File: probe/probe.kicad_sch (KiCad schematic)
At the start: 4 parts, among them J1 To circuit, J2 To scope

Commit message: Update based on first constructed version
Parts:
- added C2: 5pF, Capacitor_SMD:C_0805_2012Metric, symbol Device:C
- added R2: 4.5MΩ, Resistor_SMD:R_0805_2012Metric_Pad1.20x1.40mm_HandSolder, symbol Device:R
- R1: value 9MΩ -> 4.5MΩ
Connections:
- net In: now reaches C1.1, J1.1 (In), R1.1
- net In: now also C2.1
- net Out: now reaches C1.2, J2.1 (In)
- net Out: now also C2.2, R2.2; no longer R1.2
- new net: R1.2, R2.1
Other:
- moved on the sheet: R1
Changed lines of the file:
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@@
 	(paper "A4")
+	(junction
+		(at 119.38 87.63)
+		(diameter 0)
+		(color 0 0 0 0)
+	)
 	(junction
 		(at 119.38 80.01)
@@
 		(color 0 0 0 0)
 	)
+	(junction
+		(at 138.43 87.63)
+		(diameter 0)
+		(color 0 0 0 0)
+	)
 	(wire
 		(pts
@@
 	(wire
 		(pts
-			(xy 119.38 80.01) (xy 124.46 80.01)
+			(xy 119.38 80.01) (xy 120.65 80.01)
 		)
 		(stroke
@@
 	(wire
 		(pts
+			(xy 132.08 97.79) (xy 138.43 97.79)
+		)
+		(stroke
+			(width 0)
+			(type default)
+		)
+	)
+	(wire
+		(pts
 			(xy 119.38 80.01) (xy 119.38 87.63)
 		)
@@
 	(wire
 		(pts
-			(xy 132.08 80.01) (xy 138.43 80.01)
+			(xy 138.43 87.63) (xy 138.43 97.79)
+		)
+		(stroke
+			(width 0)
+			(type default)
+		)
+	)
+	(wire
+		(pts
+			(xy 128.27 80.01) (xy 129.54 80.01)
+		)
+		(stroke
+			(width 0)
+			(type default)
+		)
+	)
+	(wire
+		(pts
+			(xy 119.38 87.63) (xy 119.38 97.79)
+		)
+		(stroke
+			(width 0)
+			(type default)
+		)
+	)
+	(wire
+		(pts
+			(xy 124.46 97.79) (xy 119.38 97.79)
 		)
 		(stroke
@@
 	(wire
 		(pts
+			(xy 137.16 80.01) (xy 138.43 80.01)
+		)
+		(stroke
+			(width 0)
+			(type default)
+		)
+	)
+	(wire
+		(pts
 			(xy 152.4 85.09) (xy 152.4 90.17)
 		)
@@
 			(width 0)
 			(type default)
+		)
+	)
+	(label "In"
+		(at 111.76 80.01 0)
+		(effects
+			(font
+				(size 1.27 1.27)
+			)
+			(justify left bottom)
+		)
+	)
+	(label "Out"
+		(at 140.97 80.01 0)
+		(effects
+			(font
+				(size 1.27 1.27)
+			)
+			(justify left bottom)
 		)
 	)
@@
 	)
 	(symbol
+		(lib_id "Device:R")
+		(at 133.35 80.01 90)
+		(unit 1)
+		(exclude_from_sim no)
+		(in_bom yes)
+		(on_board yes)
+		(dnp no)
+		(fields_autoplaced yes)
+		(property "Reference" "R2"
+			(at 133.35 73.66 90)
+			(effects
+				(font
+					(size 1.27 1.27)
+				)
+			)
+		)
+		(property "Value" "4.5MΩ"
+			(at 133.35 76.2 90)
+			(effects
+				(font
+					(size 1.27 1.27)
+				)
+			)
+		)
+		(property "Footprint" "Resistor_SMD:R_0805_2012Metric_Pad1.20x1.40mm_HandSolder"
+			(at 133.35 81.788 90)
+			(effects
+				(font
+					(size 1.27 1.27)
+				)
+				(hide yes)
+			)
+		)
+		(property "Datasheet" "~"
+			(at 133.35 80.01 0)
+			(effects
+				(font
+					(size 1.27 1.27)
+				)
+				(hide yes)
+			)
+		)
+		(property "Description" "Resistor"
+			(at 133.35 80.01 0)
+			(effects
+				(font
+					(size 1.27 1.27)
+				)
+				(hide yes)
+			)
+		)
+		(pin "2"
+		)
+		(pin "1"
+		)
+		(instances
+			(project "probe"
+				(path "/0e2e18e6-1bf7-45b9-957f-fc4f8daaef3f"
+					(reference "R2")
+					(unit 1)
+				)
+			)
+		)
+	)
+	(symbol
 		(lib_id "power:GND")
 		(at 152.4 90.17 0)
@@
 	)
 	(symbol
+		(lib_id "Device:C")
+		(at 128.27 97.79 90)
+		(unit 1)
+		(exclude_from_sim no)
+		(in_bom yes)
+		(on_board yes)
+		(dnp no)
+		(property "Reference" "C2"
+			(at 128.27 101.6 90)
+			(effects
+				(font
+					(size 1.27 1.27)
+				)
+			)
+		)
+		(property "Value" "5pF"
+			(at 128.524 103.632 90)
+			(effects
+				(font
+					(size 1.27 1.27)
+				)
+			)
+		)
+		(property "Footprint" "Capacitor_SMD:C_0805_2012Metric"
+			(at 132.08 96.8248 0)
+			(effects
+				(font
+					(size 1.27 1.27)
+				)
+				(hide yes)
+			)
+		)
+		(property "Datasheet" "~"
+			(at 128.27 97.79 0)
+			(effects
+				(font
+					(size 1.27 1.27)
+				)
+				(hide yes)
+			)
+		)
+		(property "Description" "Unpolarized capacitor"
+			(at 128.27 97.79 0)
+			(effects
+				(font
+					(size 1.27 1.27)
+				)
+				(hide yes)
+			)
+		)
+		(pin "1"
+		)
+		(pin "2"
+		)
+		(instances
+			(project "probe"
+				(path "/0e2e18e6-1bf7-45b9-957f-fc4f8daaef3f"
+					(reference "C2")
+					(unit 1)
+				)
+			)
+		)
+	)
+	(symbol
 		(lib_id "Device:R")
-		(at 128.27 80.01 90)
+		(at 124.46 80.01 90)
 		(unit 1)
 		(exclude_from_sim no)
@@
 		(fields_autoplaced yes)
 		(property "Reference" "R1"
-			(at 128.27 73.66 90)
-			(effects
-				(font
-					(size 1.27 1.27)
-				)
-			)
-		)
-		(property "Value" "9MΩ"
-			(at 128.27 76.2 90)
+			(at 124.46 73.66 90)
+			(effects
+				(font
+					(size 1.27 1.27)
+				)
+			)
+		)
+		(property "Value" "4.5MΩ"
+			(at 124.46 76.2 90)
 			(effects
 				(font
@@
 		)
 		(property "Footprint" "Resistor_SMD:R_0805_2012Metric_Pad1.20x1.40mm_HandSolder"
-			(at 128.27 81.788 90)
+			(at 124.46 81.788 90)
 			(effects
 				(font
@@
 		)
 		(property "Datasheet" "~"
-			(at 128.27 80.01 0)
+			(at 124.46 80.01 0)
 			(effects
 				(font
@@
 		)
 		(property "Description" "Resistor"
-			(at 128.27 80.01 0)
-			(effects
-				(font
+			(at 124.46 80.01 0)
+			(effects
+				(font

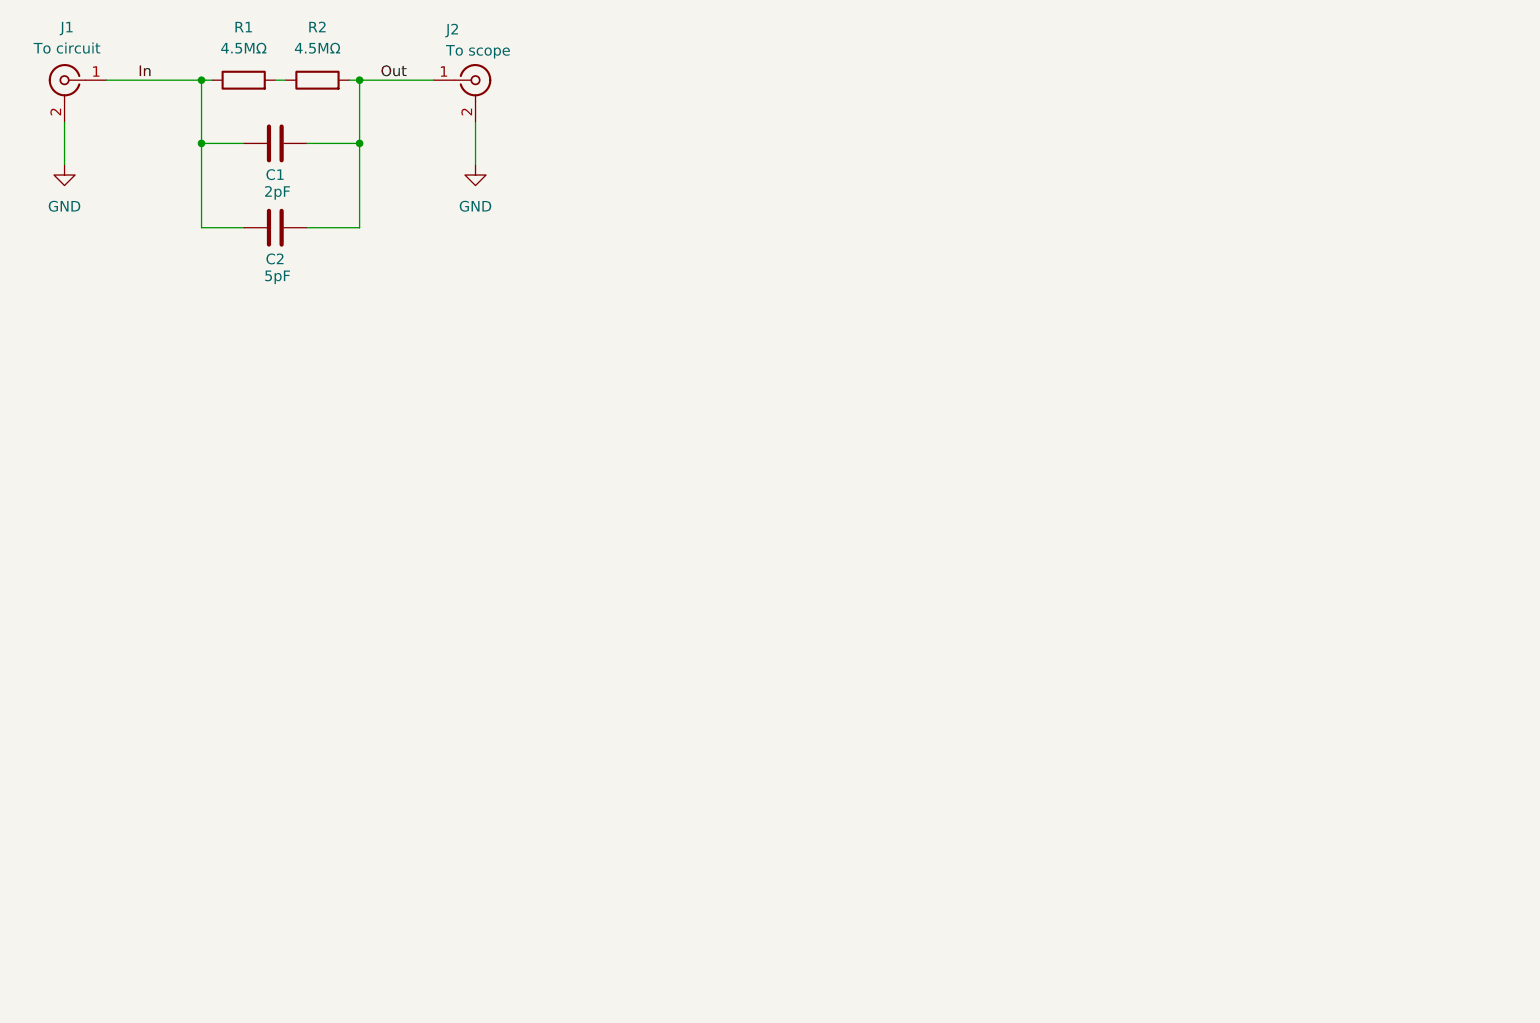
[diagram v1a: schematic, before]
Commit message: Combined both boards into single probe board
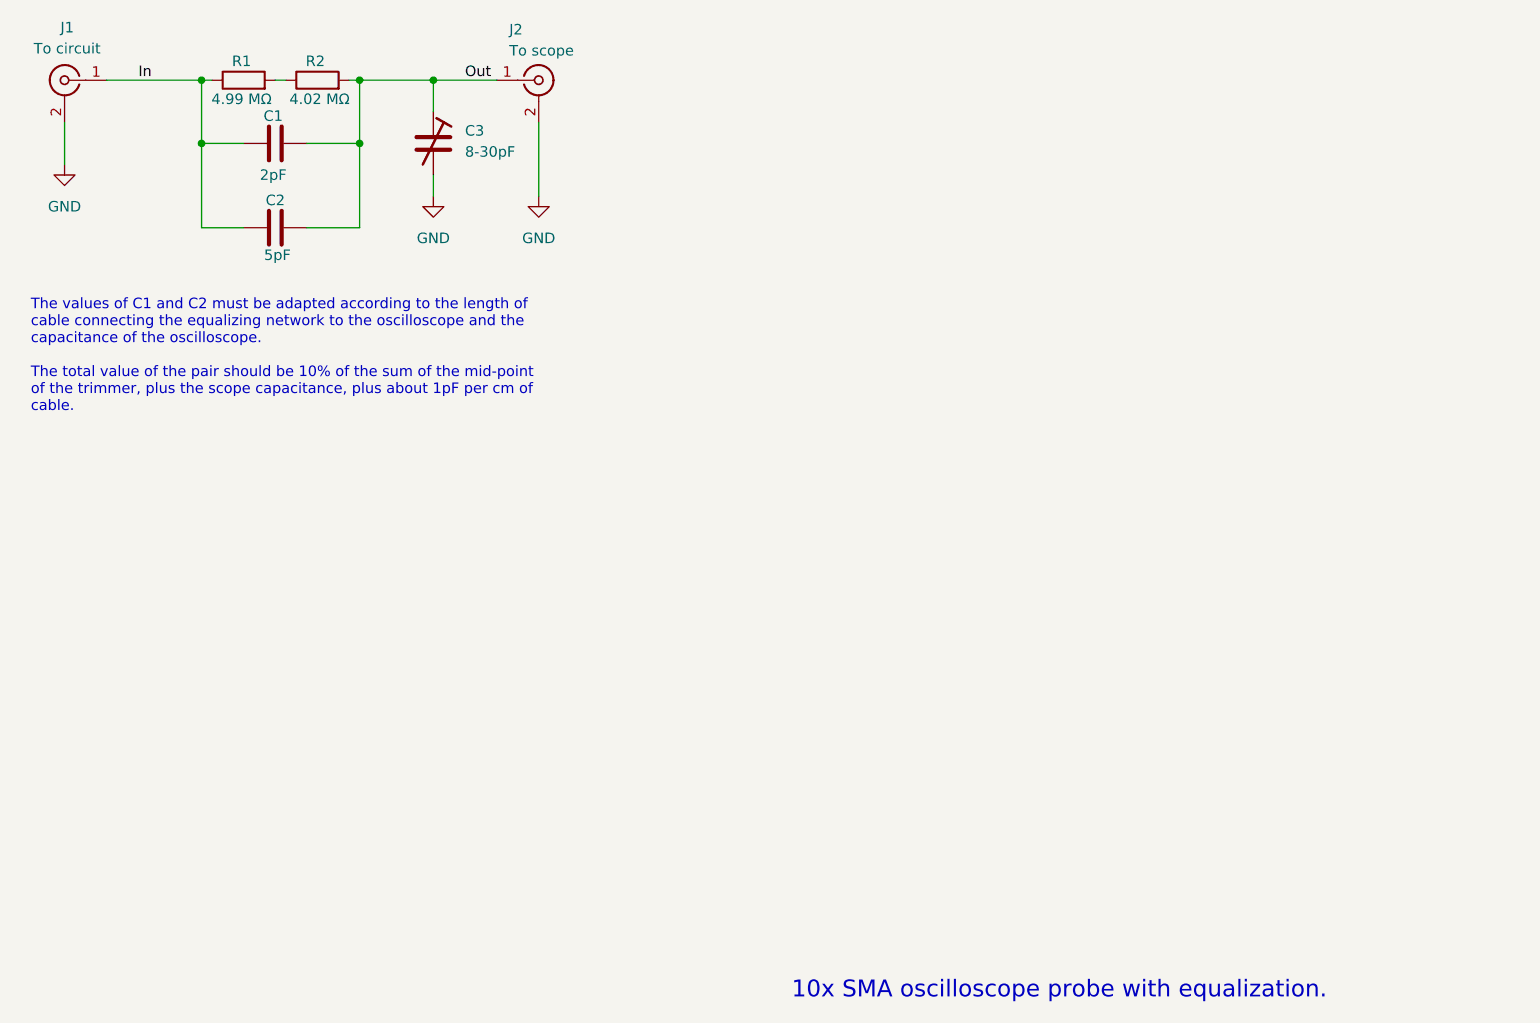
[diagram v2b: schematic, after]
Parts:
- added C3: 8-30pF, Capacitor_SMD:C_Trimmer_Sprague-Goodman_SGC3, symbol Device:C_Trim
- R1: value 4.5MΩ -> 4.99 MΩ
- R2: value 4.5MΩ -> 4.02 MΩ
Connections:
- net GND: now also C3.2
- net Out: now also C3.1
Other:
- note added: "10x SMA oscilloscope probe with equalization."
- note added: "The values of C1 and C2 must be adapted according to the length of cable connecting the equalizing network to the oscilloscope and the capacitance of the oscilloscope. The total value of the pair should be 10% of the sum of the mid-point of the trimmer, plus the scope capacitance, plus about 1pF per cm of cable."
- moved on the sheet: J2
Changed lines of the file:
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@@
 	(generator_version "9.0")
 	(paper "A4")
+	(text "The values of C1 and C2 must be adapted according to the length of \ncable connecting the equalizing network to the oscilloscope and the\ncapacitance of the oscilloscope.\n\nThe total value of the pair should be 10% of the sum of the mid-point\nof the trimmer, plus the scope capacitance, plus about 1pF per cm of\ncable."
+		(exclude_from_sim no)
+		(at 98.806 113.284 0)
+		(effects
+			(font
+				(size 1.27 1.27)
+			)
+			(justify left)
+		)
+	)
+	(text "10x SMA oscilloscope probe with equalization."
+		(exclude_from_sim no)
+		(at 190.5 189.738 0)
+		(effects
+			(font
+				(size 2.032 2.032)
+			)
+			(justify left)
+		)
+	)
 	(junction
 		(at 119.38 87.63)
@@
 	)
 	(junction
+		(at 147.32 80.01)
+		(diameter 0)
+		(color 0 0 0 0)
+	)
+	(junction
 		(at 138.43 87.63)
 		(diameter 0)
@@
 	(wire
 		(pts
+			(xy 147.32 91.44) (xy 147.32 93.98)
+		)
+		(stroke
+			(width 0)
+			(type default)
+		)
+	)
+	(wire
+		(pts
 			(xy 132.08 87.63) (xy 138.43 87.63)
 		)
@@
 	(wire
 		(pts
+			(xy 147.32 80.01) (xy 154.94 80.01)
+		)
+		(stroke
+			(width 0)
+			(type default)
+		)
+	)
+	(wire
+		(pts
+			(xy 147.32 80.01) (xy 147.32 83.82)
+		)
+		(stroke
+			(width 0)
+			(type default)
+		)
+	)
+	(wire
+		(pts
 			(xy 124.46 87.63) (xy 119.38 87.63)
 		)
@@
 	(wire
 		(pts
+			(xy 138.43 80.01) (xy 147.32 80.01)
+		)
+		(stroke
+			(width 0)
+			(type default)
+		)
+	)
+	(wire
+		(pts
 			(xy 128.27 80.01) (xy 129.54 80.01)
 		)
@@
 	(wire
 		(pts
-			(xy 138.43 80.01) (xy 147.32 80.01)
-		)
-		(stroke
-			(width 0)
-			(type default)
-		)
-	)
-	(wire
-		(pts
 			(xy 137.16 80.01) (xy 138.43 80.01)
 		)
@@
 	(wire
 		(pts
-			(xy 152.4 85.09) (xy 152.4 90.17)
+			(xy 160.02 85.09) (xy 160.02 93.98)
 		)
 		(stroke
@@
 	)
 	(label "Out"
-		(at 140.97 80.01 0)
+		(at 151.13 80.01 0)
 		(effects
 			(font
@@
 		(on_board yes)
 		(dnp no)
-		(fields_autoplaced yes)
 		(property "Reference" "R2"
-			(at 133.35 73.66 90)
-			(effects
-				(font
-					(size 1.27 1.27)
-				)
-			)
-		)
-		(property "Value" "4.5MΩ"
-			(at 133.35 76.2 90)
+			(at 133.096 77.724 90)
+			(effects
+				(font
+					(size 1.27 1.27)
+				)
+			)
+		)
+		(property "Value" "4.02 MΩ"
+			(at 133.604 82.296 90)
 			(effects
 				(font
@@
 	)
 	(symbol
+		(lib_id "Device:C_Trim")
+		(at 147.32 87.63 0)
+		(unit 1)
+		(exclude_from_sim no)
+		(in_bom yes)
+		(on_board yes)
+		(dnp no)
+		(fields_autoplaced yes)
+		(property "Reference" "C3"
+			(at 151.13 86.1059 0)
+			(effects
+				(font
+					(size 1.27 1.27)
+				)
+				(justify left)
+			)
+		)
+		(property "Value" "8-30pF"
+			(at 151.13 88.6459 0)
+			(effects
+				(font
+					(size 1.27 1.27)
+				)
+				(justify left)
+			)
+		)
+		(property "Footprint" "Capacitor_SMD:C_Trimmer_Sprague-Goodman_SGC3"
+			(at 147.32 87.63 0)
+			(effects
+				(font
+					(size 1.27 1.27)
+				)
+				(hide yes)
+			)
+		)
+		(property "Datasheet" "https://mm.digikey.com/Volume0/opasdata/d220001/medias/docus/430/SCG3S_Series_Spec_2020.pdf?_gl=1*1cjebp5*_up*MQ..*_gs*MQ..&gclid=Cj0KCQiAr5nKBhCpARIsACa_NiOp8v-3Qg6VxRsadesvz1OIcx9M1SlvFwP3e9yqGBqAxM4DujWyJmgaArtFEALw_wcB&gclsrc=aw.ds&gbraid=0AAAAADrbLlhdecwtFDHIKXDcL_djQaT_V"
+			(at 147.32 87.63 0)
+			(effects
+				(font
+					(size 1.27 1.27)
+				)
+				(hide yes)
+			)
+		)
+		(property "Description" "Trimmable capacitor"
+			(at 147.32 87.63 0)
+			(effects
+				(font
+					(size 1.27 1.27)
+				)
+				(hide yes)
+			)
+		)
+		(property "Digikey" "https://www.digikey.com/en/products/detail/ew-electronics/SGC3S300NM/11689290"
+			(at 147.32 87.63 0)
+			(effects
+				(font
+					(size 1.27 1.27)
+				)
+				(hide yes)
+			)
+		)
+		(pin "1"
+		)
+		(pin "2"
+		)
+		(instances
+			(project "probe"
+				(path "/0e2e18e6-1bf7-45b9-957f-fc4f8daaef3f"
+					(reference "C3")
+					(unit 1)
+				)
+			)
+		)
+	)
+	(symbol
 		(lib_id "power:GND")
-		(at 152.4 90.17 0)
+		(at 160.02 93.98 0)
 		(unit 1)
 		(exclude_from_sim no)
@@
 		(fields_autoplaced yes)
 		(property "Reference" "#PWR02"
-			(at 152.4 96.52 0)
+			(at 160.02 100.33 0)
 			(effects
 				(font
@@
 		)
 		(property "Value" "GND"
-			(at 152.4 95.25 0)
+			(at 160.02 99.06 0)
 			(effects
 				(font
@@
 		)
 		(property "Footprint" ""
-			(at 152.4 90.17 0)
+			(at 160.02 93.98 0)
 			(effects
 				(font
@@
 		)
 		(property "Datasheet" ""
-			(at 152.4 90.17 0)
+			(at 160.02 93.98 0)
 			(effects
 				(font
@@
 		)
 		(property "Description" "Power symbol creates a global label with name \"GND\" , ground"
-			(at 152.4 90.17 0)
+			(at 160.02 93.98 0)
 			(effects
 				(font
@@
 	(symbol
 		(lib_id "Connector:Conn_Coaxial")
-		(at 152.4 80.01 0)
+		(at 160.02 80.01 0)
 		(unit 1)
 		(exclude_from_sim no)
@@
 		(dnp no)
 		(property "Reference" "J2"
-			(at 148.844 73.914 0)
+			(at 156.464 73.914 0)
 			(effects
 				(font
@@
 		)
 		(property "Value" "To scope"
-			(at 148.844 76.454 0)
+			(at 156.464 76.454 0)
 			(effects
 				(font
@@
 		)
 		(property "Footprint" "Connector_Coaxial:SMA_Samtec_SMA-J-P-H-ST-EM1_EdgeMount"
-			(at 152.4 80.01 0)
+			(at 160.02 80.01 0)
 			(effects
 				(font
@@
 		)
 		(property "Datasheet" "~"
-			(at 152.4 80.01 0)
+			(at 160.02 80.01 0)
 			(effects
 				(font
@@
 		)
 		(property "Description" "coaxial connector (BNC, SMA, SMB, SMC, Cinch/RCA, LEMO, ...)"
-			(at 152.4 80.01 0)
+			(at 160.02 80.01 0)
 			(effects
 				(font
@@
 		(dnp no)
 		(property "Reference" "C1"
-			(at 128.27 91.44 90)
+			(at 128.016 84.328 90)
 			(effects
 				(font
@@
 		)
 		(property "Value" "2pF"
-			(at 128.524 93.472 90)
+			(at 128.016 91.44 90)
 			(effects
 				(font
@@
 		(dnp no)
 		(property "Reference" "C2"
-			(at 128.27 101.6 90)
+			(at 128.27 94.488 90)
 			(effects
 				(font
@@
 		)
 		(property "Value" "5pF"
-			(at 128.524 103.632 90)
+			(at 128.524 101.092 90)
 			(effects
 				(font
@@
 	)
 	(symbol
+		(lib_id "power:GND")
+		(at 147.32 93.98 0)
+		(unit 1)
+		(exclude_from_sim no)
+		(in_bom yes)
+		(on_board yes)
+		(dnp no)
+		(fields_autoplaced yes)
+		(property "Reference" "#PWR03"
+			(at 147.32 100.33 0)
+			(effects
+				(font
+					(size 1.27 1.27)
+				)
+				(hide yes)
+			)
+		)
+		(property "Value" "GND"
+			(at 147.32 99.06 0)
+			(effects
+				(font
+					(size 1.27 1.27)
+				)
+			)
+		)
+		(property "Footprint" ""
+			(at 147.32 93.98 0)
+			(effects
+				(font
+					(size 1.27 1.27)
+				)
+				(hide yes)
+			)
+		)
+		(property "Datasheet" ""
+			(at 147.32 93.98 0)
+			(effects
+				(font
+					(size 1.27 1.27)
+				)
+				(hide yes)
+			)
+		)
+		(property "Description" "Power symbol creates a global label with name \"GND\" , ground"
+			(at 147.32 93.98 0)
+			(effects
+				(font
+					(size 1.27 1.27)
+				)
+				(hide yes)
+			)
+		)
+		(pin "1"
+		)
+		(instances
+			(project "probe"
+				(path "/0e2e18e6-1bf7-45b9-957f-fc4f8daaef3f"
+					(reference "#PWR03")
+					(unit 1)
+				)
+			)
+		)
+	)
+	(symbol
 		(lib_id "Device:R")
 		(at 124.46 80.01 90)
@@
 		(on_board yes)
 		(dnp no)
-		(fields_autoplaced yes)
 		(property "Reference" "R1"
-			(at 124.46 73.66 90)
-			(effects
-				(font
-					(size 1.27 1.27)
-				)
-			)
-		)
-		(property "Value" "4.5MΩ"
-			(at 124.46 76.2 90)
-			(effects
-				(font
+			(at 124.206 77.724 90)
+			(effects
+				(font
+					(size 1.27 1.27)
+				)
+			)
+		)
+		(property "Value" "4.99 MΩ"
+			(at 124.206 82.296 90)
+			(effects
+				(font
